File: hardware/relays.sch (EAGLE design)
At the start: 19 parts, among them U1 MMBT2222ALT1G, U2 MMBT2222ALT1G

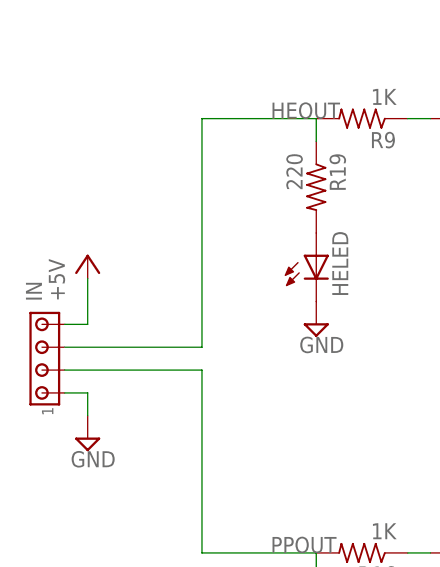
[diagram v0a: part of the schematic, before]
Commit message: IO and Relay boards are distinct
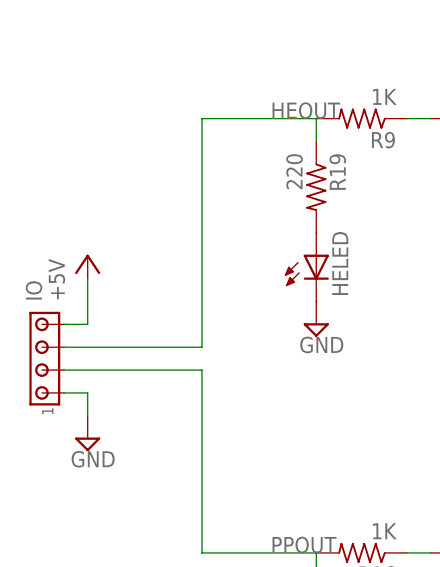
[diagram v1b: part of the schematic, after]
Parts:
- renumbered IN to IO
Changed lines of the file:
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@@
 <part name="U$4" library="digikey" deviceset="PC1725041" device=""/>
 <part name="U$6" library="digikey" deviceset="PC1719028" device=""/>
-<part name="IN" library="con-amp" library_urn="urn:adsk.eagle:library:127" deviceset="MTA04-100" device=""/>
+<part name="IO" library="con-amp" library_urn="urn:adsk.eagle:library:127" deviceset="MTA04-100" device=""/>
 <part name="P+3" library="supply1" library_urn="urn:adsk.eagle:library:371" deviceset="+5V" device=""/>
 <part name="SUPPLY1" library="supply2" deviceset="GND" device=""/>
@@
 <instance part="U$4" gate="G$1" x="340.36" y="55.88"/>
 <instance part="U$6" gate="G$1" x="340.36" y="111.76"/>
-<instance part="IN" gate="G$1" x="154.94" y="76.2" rot="R90"/>
+<instance part="IO" gate="G$1" x="154.94" y="76.2" rot="R90"/>
 <instance part="P+3" gate="1" x="160.02" y="88.9"/>
 <instance part="SUPPLY1" gate="GND" x="160.02" y="68.58"/>
@@
 </segment>
 <segment>
-<pinref part="IN" gate="G$1" pin="1"/>
+<pinref part="IO" gate="G$1" pin="1"/>
 <pinref part="SUPPLY1" gate="GND" pin="GND"/>
 <wire x1="157.48" y1="73.66" x2="160.02" y2="73.66" width="0.1524" layer="91"/>
@@
 <segment>
 <pinref part="P+3" gate="1" pin="+5V"/>
-<pinref part="IN" gate="G$1" pin="4"/>
+<pinref part="IO" gate="G$1" pin="4"/>
 <wire x1="160.02" y1="86.36" x2="160.02" y2="81.28" width="0.1524" layer="91"/>
 <wire x1="160.02" y1="81.28" x2="157.48" y2="81.28" width="0.1524" layer="91"/>
@@
 <pinref part="R19" gate="G$1" pin="1"/>
 <wire x1="185.42" y1="101.6" x2="185.42" y2="104.14" width="0.1524" layer="91"/>
-<pinref part="IN" gate="G$1" pin="3"/>
+<pinref part="IO" gate="G$1" pin="3"/>
 <wire x1="157.48" y1="78.74" x2="172.72" y2="78.74" width="0.1524" layer="91"/>
 <wire x1="172.72" y1="78.74" x2="172.72" y2="104.14" width="0.1524" layer="91"/>
@@
 <pinref part="R20" gate="G$1" pin="1"/>
 <wire x1="185.42" y1="53.34" x2="185.42" y2="55.88" width="0.1524" layer="91"/>
-<pinref part="IN" gate="G$1" pin="2"/>
+<pinref part="IO" gate="G$1" pin="2"/>
 <wire x1="157.48" y1="76.2" x2="172.72" y2="76.2" width="0.1524" layer="91"/>
 <wire x1="172.72" y1="76.2" x2="172.72" y2="55.88" width="0.1524" layer="91"/>

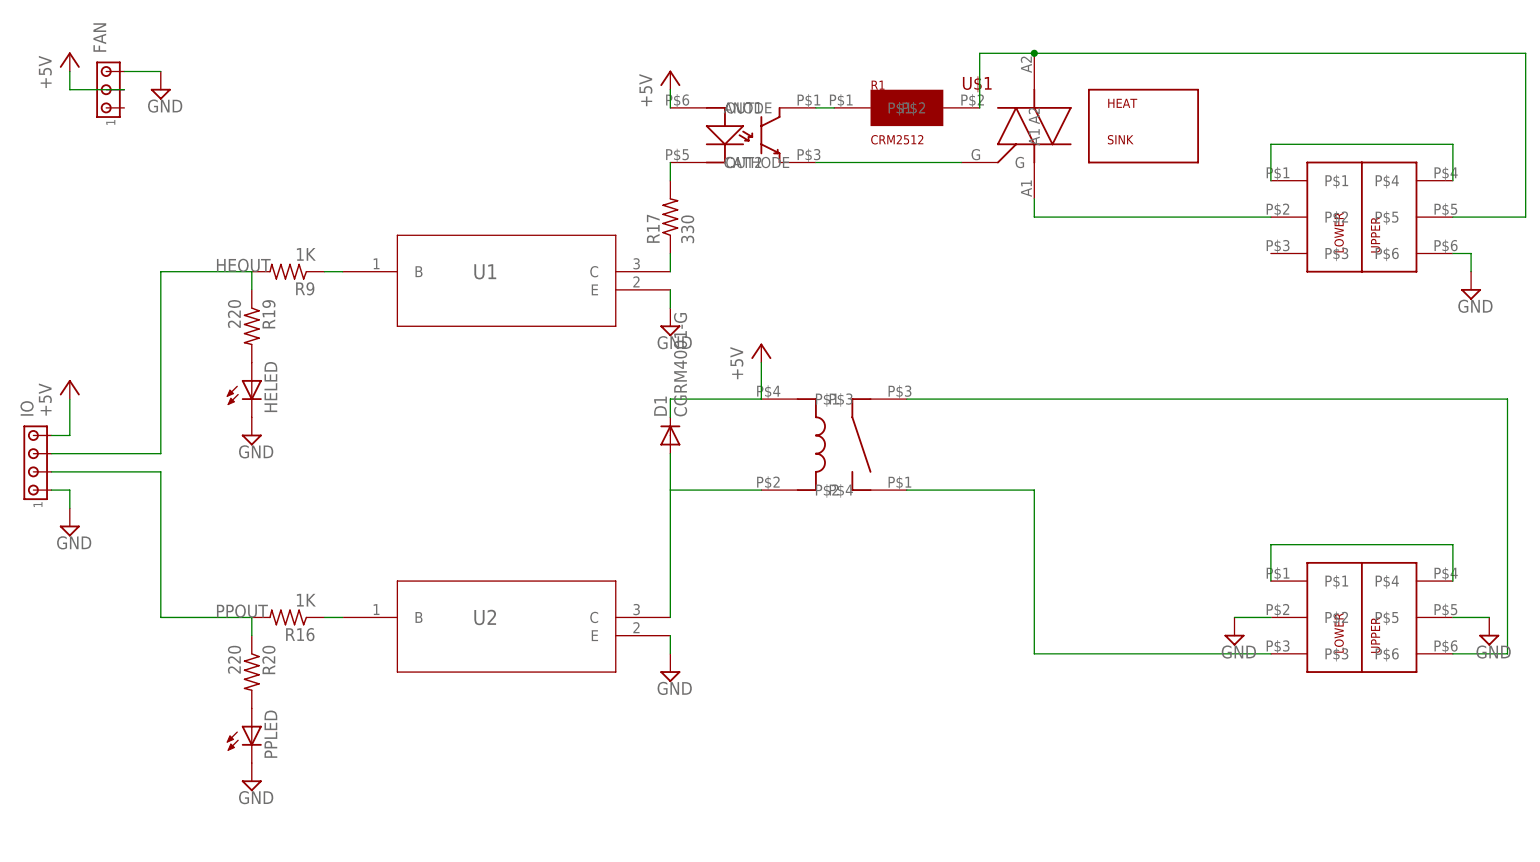
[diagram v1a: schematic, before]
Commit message: Fix relay holes, triac holes and orientation, and DRC issues.
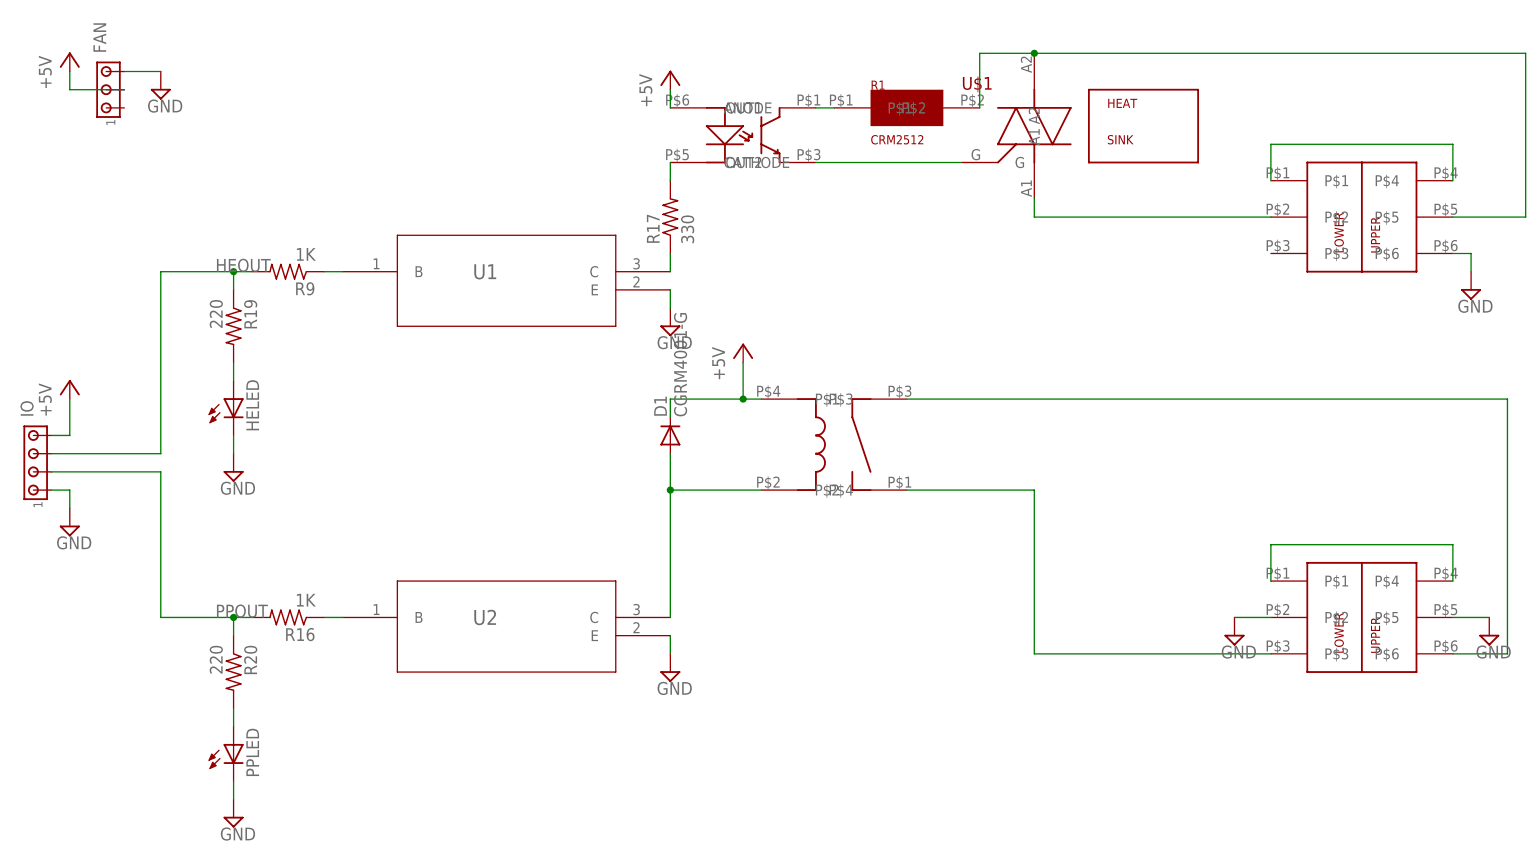
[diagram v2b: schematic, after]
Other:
- moved on the sheet: HELED, PPLED, R19, R20
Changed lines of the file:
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@@
 <instance part="R1" gate="G$1" x="276.86" y="127"/>
 <instance part="P+1" gate="1" x="243.84" y="132.08"/>
-<instance part="P+2" gate="1" x="256.54" y="93.98"/>
+<instance part="P+2" gate="1" x="254" y="93.98"/>
 <instance part="SUPPLY17" gate="GND" x="355.6" y="101.6"/>
 <instance part="SUPPLY18" gate="GND" x="358.14" y="53.34"/>
 <instance part="SUPPLY19" gate="GND" x="322.58" y="53.34"/>
 <instance part="R17" gate="G$1" x="243.84" y="111.76" rot="R90"/>
-<instance part="HELED" gate="G$1" x="185.42" y="88.9"/>
-<instance part="PPLED" gate="G$1" x="185.42" y="40.64"/>
-<instance part="R19" gate="G$1" x="185.42" y="96.52" rot="R270"/>
-<instance part="SUPPLY20" gate="GND" x="185.42" y="81.28"/>
-<instance part="SUPPLY21" gate="GND" x="185.42" y="33.02"/>
-<instance part="R20" gate="G$1" x="185.42" y="48.26" rot="R270"/>
+<instance part="HELED" gate="G$1" x="182.88" y="86.36"/>
+<instance part="PPLED" gate="G$1" x="182.88" y="38.1"/>
+<instance part="R19" gate="G$1" x="182.88" y="96.52" rot="R270"/>
+<instance part="SUPPLY20" gate="GND" x="182.88" y="76.2"/>
+<instance part="SUPPLY21" gate="GND" x="182.88" y="27.94"/>
+<instance part="R20" gate="G$1" x="182.88" y="48.26" rot="R270"/>
 <instance part="U$3" gate="G$1" x="264.16" y="81.28"/>
 <instance part="U$2" gate="G$1" x="309.88" y="124.46"/>
@@
 <pinref part="HELED" gate="G$1" pin="C"/>
 <pinref part="SUPPLY20" gate="GND" pin="GND"/>
+<wire x1="182.88" y1="78.74" x2="182.88" y2="81.28" width="0.1524" layer="91"/>
 </segment>
 <segment>
 <pinref part="PPLED" gate="G$1" pin="C"/>
 <pinref part="SUPPLY21" gate="GND" pin="GND"/>
+<wire x1="182.88" y1="30.48" x2="182.88" y2="33.02" width="0.1524" layer="91"/>
 </segment>
 <segment>
@@
 <net name="+5V" class="0">
 <segment>
-<pinref part="P+2" gate="1" pin="+5V"/>
-<wire x1="256.54" y1="86.36" x2="256.54" y2="91.44" width="0.1524" layer="91"/>
-<pinref part="U$3" gate="G$1" pin="P$1"/>
-<pinref part="D1" gate="G$1" pin="C"/>
-<wire x1="243.84" y1="83.82" x2="243.84" y2="86.36" width="0.1524" layer="91"/>
-<wire x1="243.84" y1="86.36" x2="256.54" y2="86.36" width="0.1524" layer="91"/>
-</segment>
-<segment>
 <pinref part="P+1" gate="1" pin="+5V"/>
 <pinref part="U$5" gate="G$1" pin="ANODE"/>
@@
 <wire x1="160.02" y1="129.54" x2="160.02" y2="132.08" width="0.1524" layer="91"/>
 </segment>
+<segment>
+<pinref part="U$3" gate="G$1" pin="P$1"/>
+<pinref part="D1" gate="G$1" pin="C"/>
+<wire x1="243.84" y1="83.82" x2="243.84" y2="86.36" width="0.1524" layer="91"/>
+<wire x1="243.84" y1="86.36" x2="254" y2="86.36" width="0.1524" layer="91"/>
+<pinref part="P+2" gate="1" pin="+5V"/>
+<wire x1="254" y1="86.36" x2="256.54" y2="86.36" width="0.1524" layer="91"/>
+<wire x1="254" y1="91.44" x2="254" y2="86.36" width="0.1524" layer="91"/>
+<junction x="254" y="86.36"/>
+</segment>
 </net>
 <net name="HEOUT" class="0">
@@
 <pinref part="R9" gate="G$1" pin="2"/>
 <label x="180.34" y="104.14" size="1.778" layer="95"/>
-<pinref part="R19" gate="G$1" pin="1"/>
-<wire x1="185.42" y1="101.6" x2="185.42" y2="104.14" width="0.1524" layer="91"/>
 <pinref part="IO" gate="G$1" pin="3"/>
 <wire x1="157.48" y1="78.74" x2="172.72" y2="78.74" width="0.1524" layer="91"/>
 <wire x1="172.72" y1="78.74" x2="172.72" y2="104.14" width="0.1524" layer="91"/>
-<wire x1="172.72" y1="104.14" x2="185.42" y2="104.14" width="0.1524" layer="91"/>
+<wire x1="172.72" y1="104.14" x2="182.88" y2="104.14" width="0.1524" layer="91"/>
+<pinref part="R19" gate="G$1" pin="1"/>
+<wire x1="182.88" y1="104.14" x2="185.42" y2="104.14" width="0.1524" layer="91"/>
+<wire x1="182.88" y1="101.6" x2="182.88" y2="104.14" width="0.1524" layer="91"/>
+<junction x="182.88" y="104.14"/>
 </segment>
 </net>
@@
 <pinref part="R16" gate="G$1" pin="2"/>
 <label x="180.34" y="55.88" size="1.778" layer="95"/>
-<pinref part="R20" gate="G$1" pin="1"/>
-<wire x1="185.42" y1="53.34" x2="185.42" y2="55.88" width="0.1524" layer="91"/>
 <pinref part="IO" gate="G$1" pin="2"/>
 <wire x1="157.48" y1="76.2" x2="172.72" y2="76.2" width="0.1524" layer="91"/>
 <wire x1="172.72" y1="76.2" x2="172.72" y2="55.88" width="0.1524" layer="91"/>
-<wire x1="172.72" y1="55.88" x2="185.42" y2="55.88" width="0.1524" layer="91"/>
+<wire x1="172.72" y1="55.88" x2="182.88" y2="55.88" width="0.1524" layer="91"/>
+<pinref part="R20" gate="G$1" pin="1"/>
+<wire x1="182.88" y1="55.88" x2="185.42" y2="55.88" width="0.1524" layer="91"/>
+<wire x1="182.88" y1="53.34" x2="182.88" y2="55.88" width="0.1524" layer="91"/>
+<junction x="182.88" y="55.88"/>
 </segment>
 </net>
@@
 <wire x1="243.84" y1="73.66" x2="243.84" y2="78.74" width="0.1524" layer="91"/>
 <wire x1="243.84" y1="55.88" x2="243.84" y2="73.66" width="0.1524" layer="91"/>
+<junction x="243.84" y="73.66"/>
 </segment>
 </net>
@@
 <pinref part="HELED" gate="G$1" pin="A"/>
 <pinref part="R19" gate="G$1" pin="2"/>
+<wire x1="182.88" y1="91.44" x2="182.88" y2="88.9" width="0.1524" layer="91"/>
 </segment>
 </net>
@@
 <pinref part="R20" gate="G$1" pin="2"/>
 <pinref part="PPLED" gate="G$1" pin="A"/>
+<wire x1="182.88" y1="43.18" x2="182.88" y2="40.64" width="0.1524" layer="91"/>
 </segment>
 </net>
@@
 </sheet>
 </sheets>
-<errors>
-</errors>
 </schematic>
 </drawing>
